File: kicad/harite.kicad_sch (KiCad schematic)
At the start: 10 parts, among them J1 503480-0500, J2 5034801000, J3 5034801000, U3 Raspberry_Pi_Pico

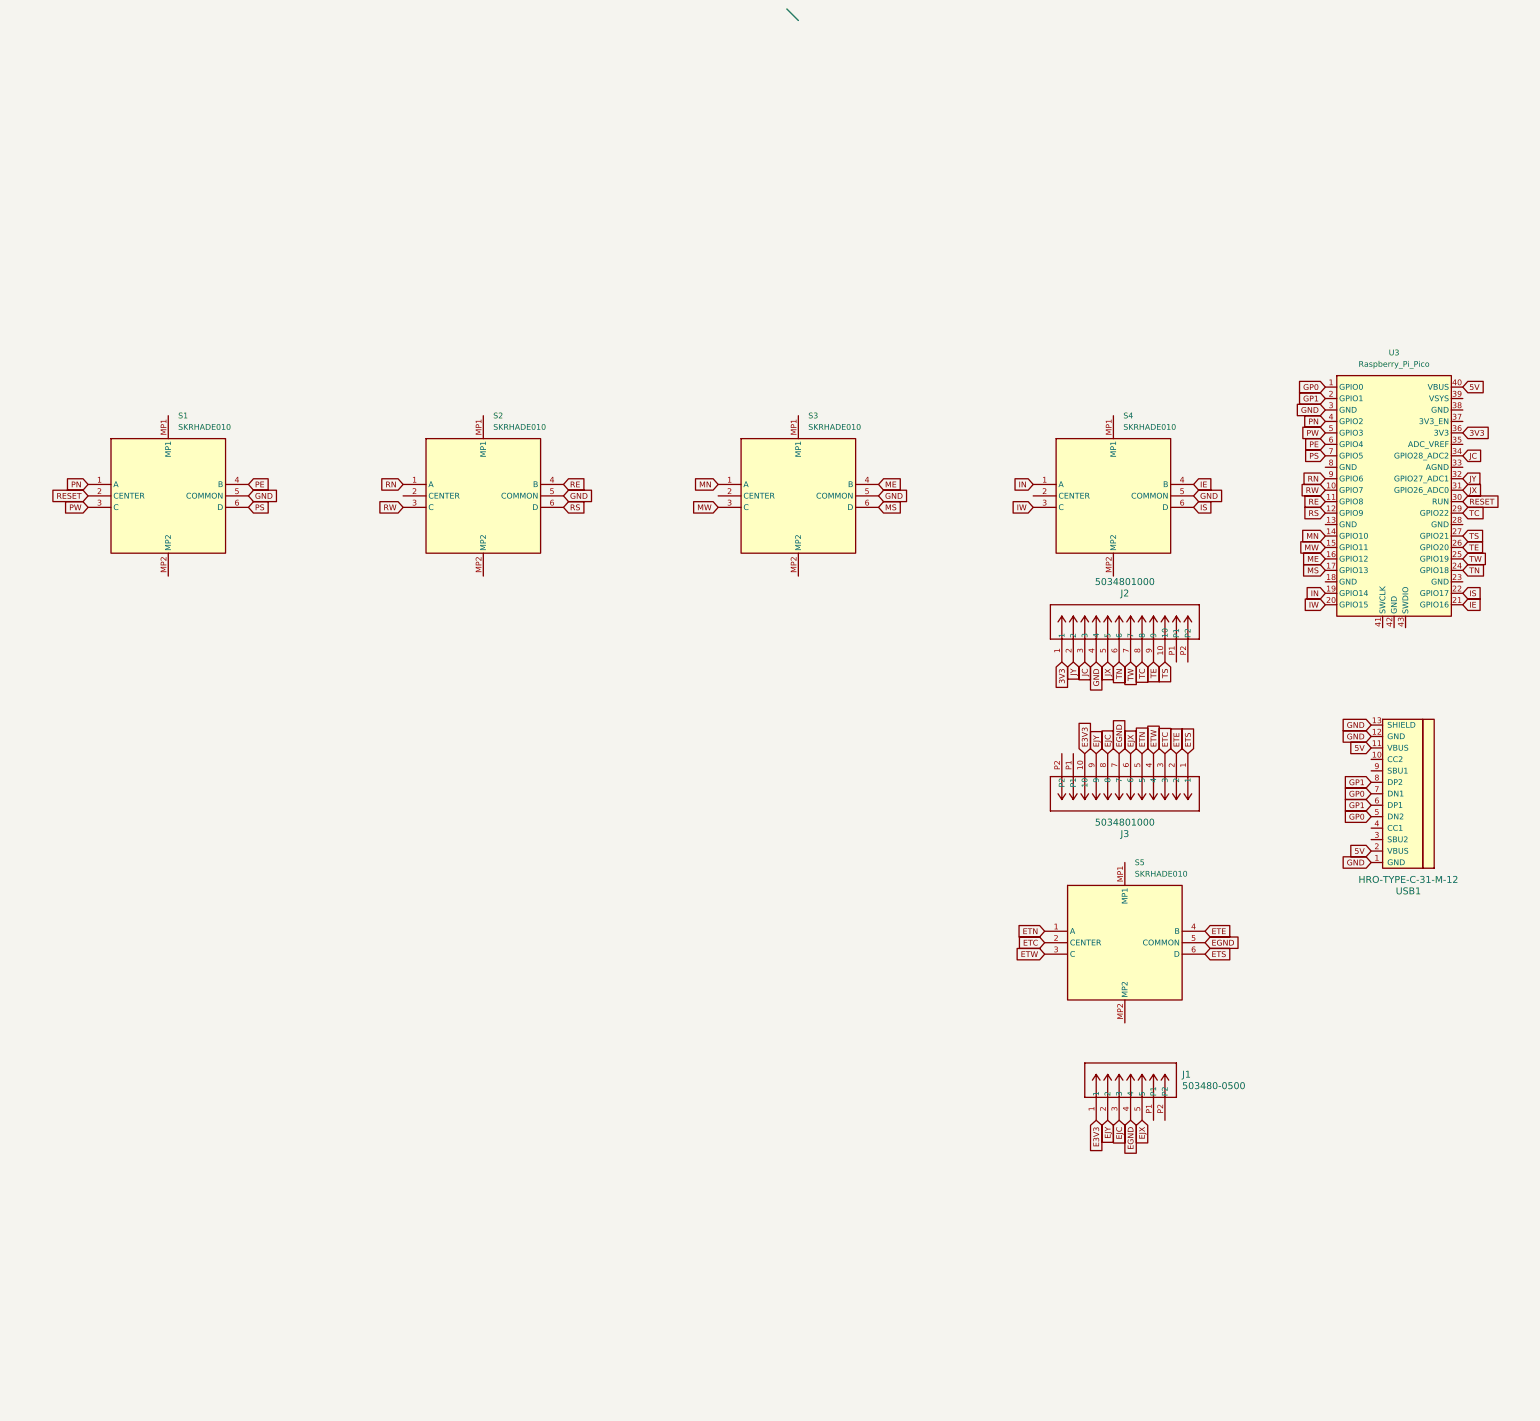
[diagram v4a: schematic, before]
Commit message: Switch back to rp2040 zero
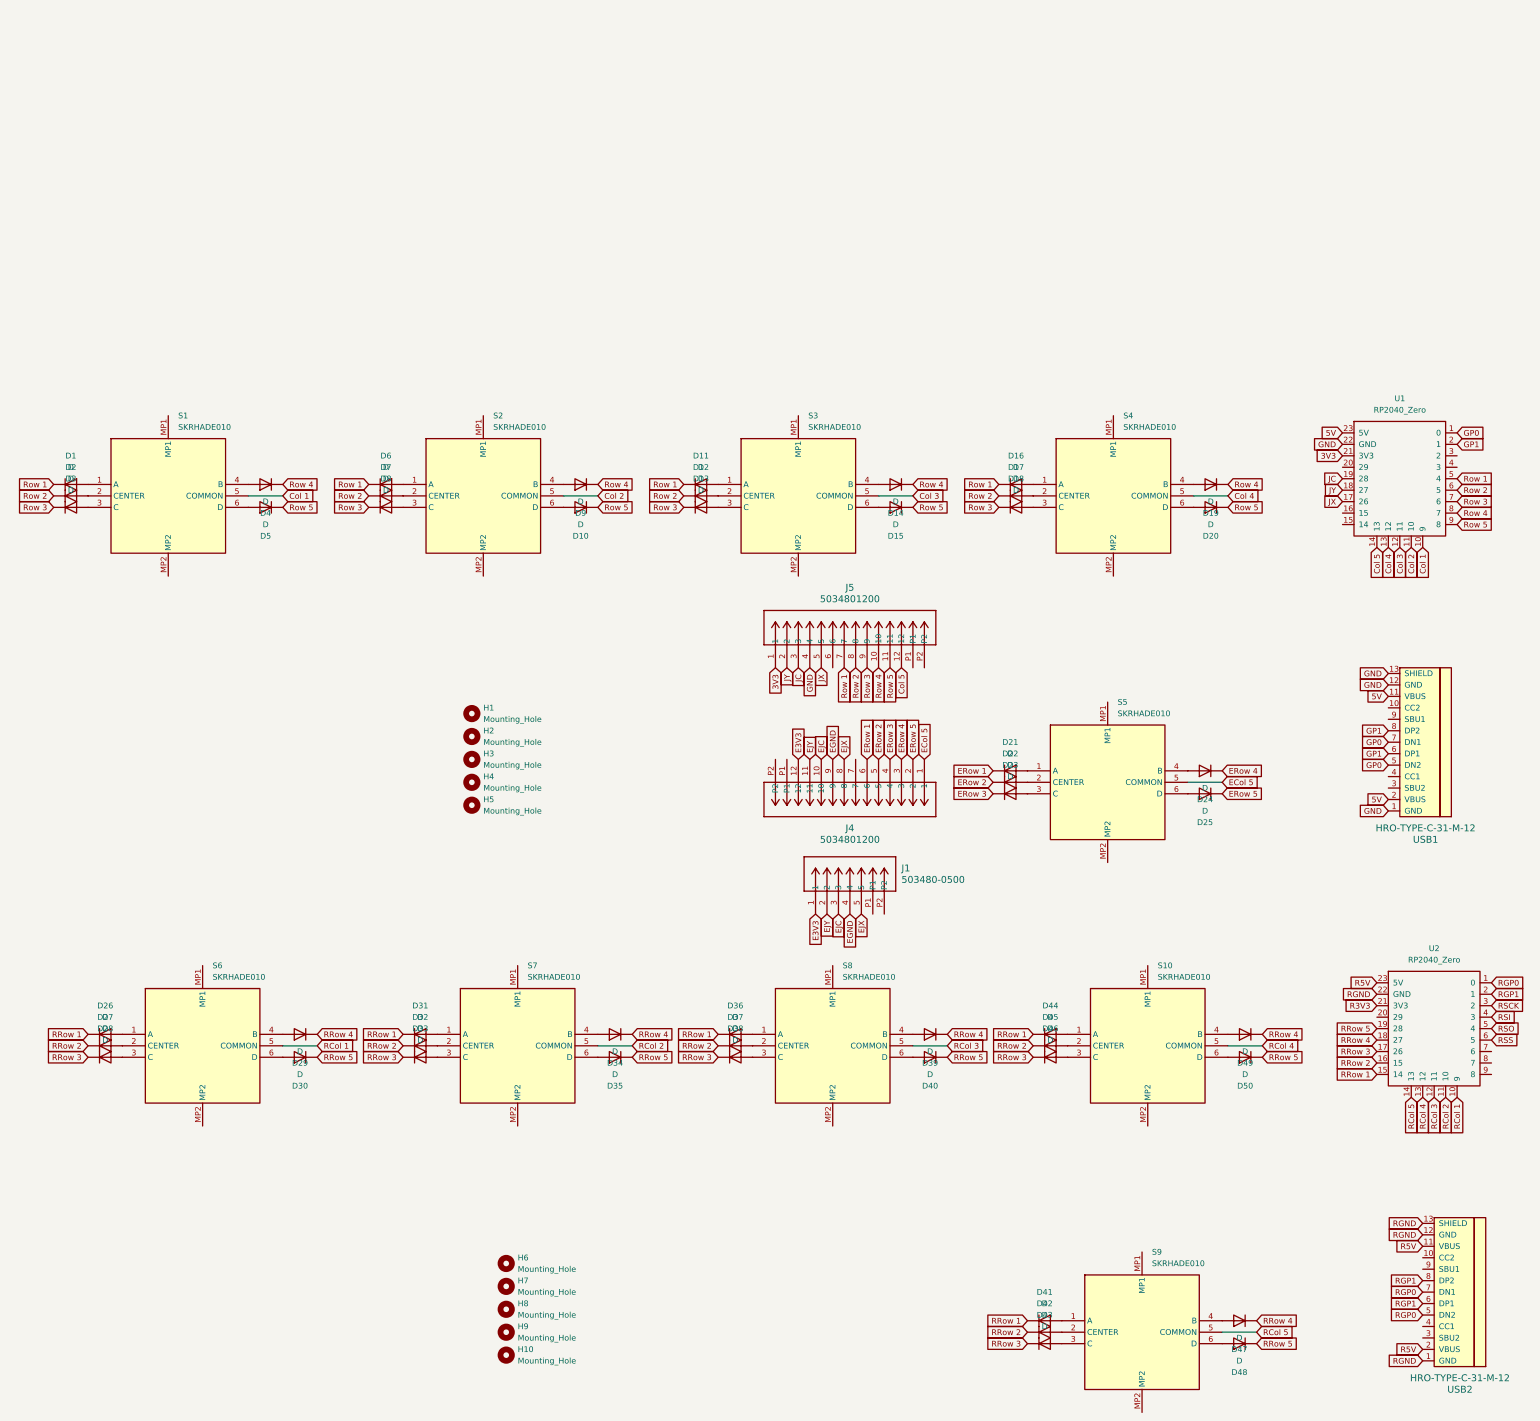
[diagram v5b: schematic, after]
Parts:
- removed J2, J3: 5034801000, 5034801000, symbol 5034801000:5034801000
- removed U3: Raspberry_Pi_Pico, ScottoKeebs_MCU:Raspberry_Pi_Pico, symbol ScottoKeebs:MCU_Raspberry_Pi_Pico
- added D1, D10, D11, D12, D13, D14, D15, D16, D17, D18, D19, D2, D20, D21, D22, D23, D24, D25, D26, D27, D28, D29, D3, D30, D31, D32, D33, D34, D35, D36, D37, D38, D39, D4, D40, D41, D42, D43, D44, D45, D46, D47, D48, D49, D5, D50, D6, D7, D8, D9: D, ScottoKeebs_Components:Diode_SOD-123, symbol Device:D
- added H1, H10, H2, H3, H4, H5, H6, H7, H8, H9: Mounting_Hole, MountingHole:MountingHole_2.2mm_M2_Pad_Via, symbol ScottoKeebs:Placeholder_Mounting_Hole
- added J4, J5: 5034801200, 5034801200, symbol 5034801200:5034801200
- added S10, S6, S7, S8, S9: SKRHADE010, footprints:SKRHADE, symbol SKRHADE010:SKRHADE010
- added U1, U2: RP2040_Zero, ScottoKeebs_MCU:RP2040_Zero, symbol ScottoKeebs:MCU_RP2040_Zero
- added USB2: HRO-TYPE-C-31-M-12, footprints:HRO-TYPE-C-31-M-12, symbol USBType-C:HRO-TYPE-C-31-M-12
- S1, S2, S3, S4, S5: footprint SKRHADE010 -> footprints:SKRHADE
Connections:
- net 3V3: now also J5.1, U1.21 (3V3)
- net 5V: now also U1.23 (5V)
- net E3V3: now also J4.12
- net EGND: now also J4.9; no longer S5.5 (COMMON)
- net EJC: now also J4.10
- net EJX: now also J4.8
- net EJY: now also J4.11
- net GND: now also J5.4, U1.22 (GND); no longer S1.5 (COMMON), S2.5 (COMMON), S3.5 (COMMON), S4.5 (COMMON)
- net GP0: now also U1.1 (0)
- net GP1: now also U1.2 (1)
- net JC: now also J5.3, U1.19 (28)
- net JX: now also J5.5, U1.17 (26)
- net JY: now also J5.2, U1.18 (27)
- net at S2.2 (CENTER): now also D7.2 (A)
- net at S3.2 (CENTER): now also D12.2 (A)
- net at S4.2 (CENTER): now also D17.2 (A)
- net ETC: no longer names the net of S5.2 (CENTER)
- net ETC: now also D22.2 (A)
- net ETE: no longer names the net of S5.4 (B)
- net ETE: now also D24.2 (A)
- net ETN: no longer names the net of S5.1 (A)
- net ETN: now also D21.2 (A)
- net ETS: no longer names the net of S5.6 (D)
- net ETS: now also D25.2 (A)
- net ETW: no longer names the net of S5.3 (C)
- net ETW: now also D23.2 (A)
- net IE: no longer names the net of S4.4 (B)
- net IE: now also D19.2 (A)
- net IN: no longer names the net of S4.1 (A)
- net IN: now also D16.2 (A)
- net IS: no longer names the net of S4.6 (D)
- net IS: now also D20.2 (A)
- net IW: no longer names the net of S4.3 (C)
- net IW: now also D18.2 (A)
- net ME: no longer names the net of S3.4 (B)
- net ME: now also D14.2 (A)
- net MN: no longer names the net of S3.1 (A)
- net MN: now also D11.2 (A)
- net MS: no longer names the net of S3.6 (D)
- net MS: now also D15.2 (A)
- net MW: no longer names the net of S3.3 (C)
- net MW: now also D13.2 (A)
- net PE: no longer names the net of S1.4 (B)
- net PE: now also D4.2 (A)
- net PN: no longer names the net of S1.1 (A)
- net PN: now also D1.2 (A)
- net PS: no longer names the net of S1.6 (D)
- net PS: now also D5.2 (A)
- net PW: no longer names the net of S1.3 (C)
- net PW: now also D3.2 (A)
- net RE: no longer names the net of S2.4 (B)
- net RE: now also D9.2 (A)
- net RESET: no longer names the net of S1.2 (CENTER)
- net RESET: now also D2.2 (A)
- net RN: no longer names the net of S2.1 (A)
- net RN: now also D6.2 (A)
- net RS: no longer names the net of S2.6 (D)
- net RS: now also D10.2 (A)
- net RW: no longer names the net of S2.3 (C)
- net RW: now also D8.2 (A)
- new net: D36.2 (A), S8.1 (A)
- new net: D37.2 (A), S8.2 (CENTER)
- new net: D38.2 (A), S8.3 (C)
- new net: D39.2 (A), S8.4 (B)
- new net: D40.2 (A), S8.6 (D)
- new net: D35.2 (A), S7.6 (D)
- new net: D45.2 (A), S10.2 (CENTER)
- new net: D44.2 (A), S10.1 (A)
- new net: D46.2 (A), S10.3 (C)
- new net: D49.2 (A), S10.4 (B)
- new net: D50.2 (A), S10.6 (D)
- new net: D41.2 (A), S9.1 (A)
- new net: D31.2 (A), S7.1 (A)
- new net: D43.2 (A), S9.3 (C)
- new net: D27.2 (A), S6.2 (CENTER)
- new net: D42.2 (A), S9.2 (CENTER)
- new net: D30.2 (A), S6.6 (D)
- new net: D34.2 (A), S7.4 (B)
- new net: D47.2 (A), S9.4 (B)
- new net: D32.2 (A), S7.2 (CENTER)
- new net: D33.2 (A), S7.3 (C)
- new net: D26.2 (A), S6.1 (A)
- new net: D48.2 (A), S9.6 (D)
- new net: D28.2 (A), S6.3 (C)
- new net: D29.2 (A), S6.4 (B)
- new net Col 1: S1.5 (COMMON), U1.10 (9)
- new net Col 2: S2.5 (COMMON), U1.11 (10)
- new net Col 3: S3.5 (COMMON), U1.12 (11)
- new net Col 4: S4.5 (COMMON), U1.13 (12)
- new net Col 5: J5.12, U1.14 (13)
- new net ECol 5: J4.1, S5.5 (COMMON)
- new net ERow 1: D21.1 (K), J4.6
- new net ERow 2: D22.1 (K), J4.5
- new net ERow 3: D23.1 (K), J4.4
- new net ERow 4: D24.1 (K), J4.3
- new net ERow 5: D25.1 (K), J4.2
- new net R3V3: U2.21 (3V3)
- new net R5V: U2.23 (5V), USB2.11 (VBUS), USB2.2 (VBUS)
- new net RCol 1: S6.5 (COMMON), U2.10 (9)
- new net RCol 2: S7.5 (COMMON), U2.11 (10)
- new net RCol 3: S8.5 (COMMON), U2.12 (11)
- new net RCol 4: S10.5 (COMMON), U2.13 (12)
- new net RCol 5: S9.5 (COMMON), U2.14 (13)
- new net RGND: U2.22 (GND), USB2.1 (GND), USB2.12 (GND), USB2.13 (SHIELD)
- new net RGP0: U2.1 (0), USB2.5 (DN2), USB2.7 (DN1)
- new net RGP1: U2.2 (1), USB2.6 (DP1), USB2.8 (DP2)
- new net RRow 1: D26.1 (K), D31.1 (K), D36.1 (K), D41.1 (K), D44.1 (K), U2.15 (14)
- new net RRow 2: D27.1 (K), D32.1 (K), D37.1 (K), D42.1 (K), D45.1 (K), U2.16 (15)
- new net RRow 3: D28.1 (K), D33.1 (K), D38.1 (K), D43.1 (K), D46.1 (K), U2.17 (26)
- new net RRow 4: D29.1 (K), D34.1 (K), D39.1 (K), D47.1 (K), D49.1 (K), U2.18 (27)
- new net RRow 5: D30.1 (K), D35.1 (K), D40.1 (K), D48.1 (K), D50.1 (K), U2.19 (28)
- new net RSCK: U2.3 (2)
- new net RSI: U2.4 (3)
- new net RSO: U2.5 (4)
- new net RSS: U2.6 (5)
- new net Row 1: D1.1 (K), D11.1 (K), D16.1 (K), D6.1 (K), J5.7, U1.5 (4)
- new net Row 2: D12.1 (K), D17.1 (K), D2.1 (K), D7.1 (K), J5.8, U1.6 (5)
- new net Row 3: D13.1 (K), D18.1 (K), D3.1 (K), D8.1 (K), J5.9, U1.7 (6)
- new net Row 4: D14.1 (K), D19.1 (K), D4.1 (K), D9.1 (K), J5.10, U1.8 (7)
- new net Row 5: D10.1 (K), D15.1 (K), D20.1 (K), D5.1 (K), J5.11, U1.9 (8)
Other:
- moved on the sheet: USB1

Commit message: update
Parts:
- added J2: Wired Joystick, Wired-Joystick, symbol Connector:Conn_01x05_Pin
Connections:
- net E3V3: now also J2.1 (Pin_1)
- net EGND: now also J2.4 (Pin_4)
- net EJC: now also J2.3 (Pin_3)
- net EJX: now also J2.5 (Pin_5)
- net EJY: now also J2.2 (Pin_2)
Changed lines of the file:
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@@
 		)
 	)
+	(global_label "EJY"
+		(shape input)
+		(at 162.56 133.35 90)
+		(fields_autoplaced yes)
+		(effects
+			(font
+				(size 1.27 1.27)
+			)
+			(justify left)
+		)
+		(property "Intersheetrefs" "${INTERSHEET_REFS}"
+			(at 162.56 127.1596 90)
+			(effects
+				(font
+					(size 1.27 1.27)
+				)
+				(justify left)
+				(hide yes)
+			)
+		)
+	)
 	(global_label "RCol 3"
 		(shape input)
@@
 		)
 	)
+	(global_label "E3V3"
+		(shape input)
+		(at 160.02 133.35 90)
+		(fields_autoplaced yes)
+		(effects
+			(font
+				(size 1.27 1.27)
+			)
+			(justify left)
+		)
+		(property "Intersheetrefs" "${INTERSHEET_REFS}"
+			(at 160.02 125.7082 90)
+			(effects
+				(font
+					(size 1.27 1.27)
+				)
+				(justify left)
+				(hide yes)
+			)
+		)
+	)
 	(global_label "JX"
 		(shape input)
@@
 		)
 	)
+	(global_label "EJC"
+		(shape input)
+		(at 165.1 133.35 90)
+		(fields_autoplaced yes)
+		(effects
+			(font
+				(size 1.27 1.27)
+			)
+			(justify left)
+		)
+		(property "Intersheetrefs" "${INTERSHEET_REFS}"
+			(at 165.1 126.9782 90)
+			(effects
+				(font
+					(size 1.27 1.27)
+				)
+				(justify left)
+				(hide yes)
+			)
+		)
+	)
 	(global_label "JC"
 		(shape input)
@@
 		)
 	)
+	(global_label "EJX"
+		(shape input)
+		(at 170.18 133.35 90)
+		(fields_autoplaced yes)
+		(effects
+			(font
+				(size 1.27 1.27)
+			)
+			(justify left)
+		)
+		(property "Intersheetrefs" "${INTERSHEET_REFS}"
+			(at 170.18 127.0387 90)
+			(effects
+				(font
+					(size 1.27 1.27)
+				)
+				(justify left)
+				(hide yes)
+			)
+		)
+	)
 	(global_label "Col 3"
 		(shape input)
@@
 		)
 	)
+	(global_label "EGND"
+		(shape input)
+		(at 167.64 133.35 90)
+		(fields_autoplaced yes)
+		(effects
+			(font
+				(size 1.27 1.27)
+			)
+			(justify left)
+		)
+		(property "Intersheetrefs" "${INTERSHEET_REFS}"
+			(at 167.64 125.3453 90)
+			(effects
+				(font
+					(size 1.27 1.27)
+				)
+				(justify left)
+				(hide yes)
+			)
+		)
+	)
 	(global_label "Row 5"
 		(shape input)
@@
 					(unit 1)
 				)
+			)
+		)
+	)
+	(symbol
+		(lib_id "Connector:Conn_01x05_Pin")
+		(at 165.1 138.43 90)
+		(unit 1)
+		(exclude_from_sim no)
+		(in_bom yes)
+		(on_board yes)
+		(dnp no)
+		(fields_autoplaced yes)
+		(property "Reference" "J2"
+			(at 165.1 140.97 90)
+			(effects
+				(font
+					(size 1.27 1.27)
+				)
+			)
+		)
+		(property "Value" "Wired Joystick"
+			(at 165.1 143.51 90)
+			(effects
+				(font
+					(size 1.27 1.27)
+				)
+			)
+		)
+		(property "Footprint" "Wired-Joystick"
+			(at 165.1 138.43 0)
+			(effects
+				(font
+					(size 1.27 1.27)
+				)
+				(hide yes)
+			)
+		)
+		(property "Datasheet" "~"
+			(at 165.1 138.43 0)
+			(effects
+				(font
+					(size 1.27 1.27)
+				)
+				(hide yes)
+			)
+		)
+		(property "Description" "Generic connector, single row, 01x05, script generated"
+			(at 165.1 138.43 0)
+			(effects
+				(font
+					(size 1.27 1.27)
+				)
+				(hide yes)
+			)
+		)
+		(pin "4"
+		)
+		(pin "3"
+		)
+		(pin "2"
+		)
+		(pin "1"
+		)
+		(pin "5"
+		)
+		(instances
+			(project "harite"
+				(path "/feb70c3f-3e34-4f8f-9694-07d231f2d237"
+					(reference "J2")
+					(unit 1)
+				)
